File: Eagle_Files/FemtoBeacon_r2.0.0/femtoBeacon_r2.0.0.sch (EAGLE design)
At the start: 60 parts

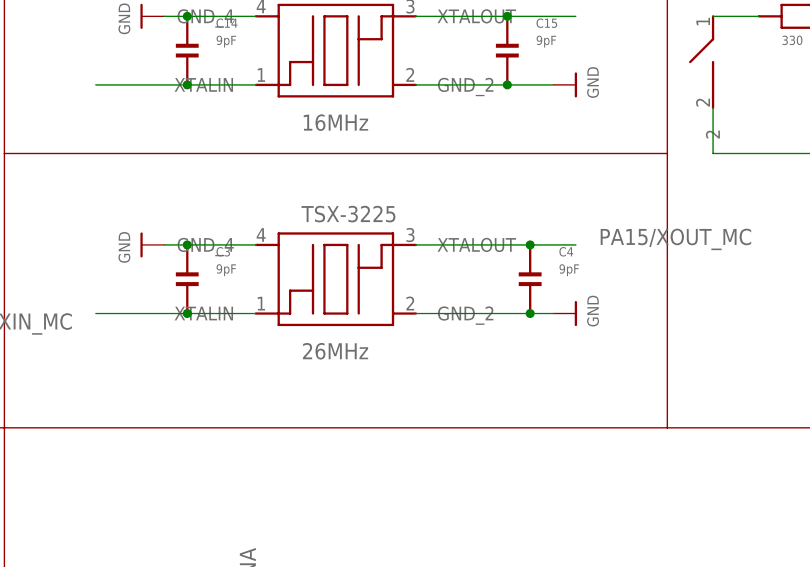
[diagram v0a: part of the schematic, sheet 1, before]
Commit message: Committing current work on FemtoBeacon (zigbee/mesh) r2.0.1, and USB dongle
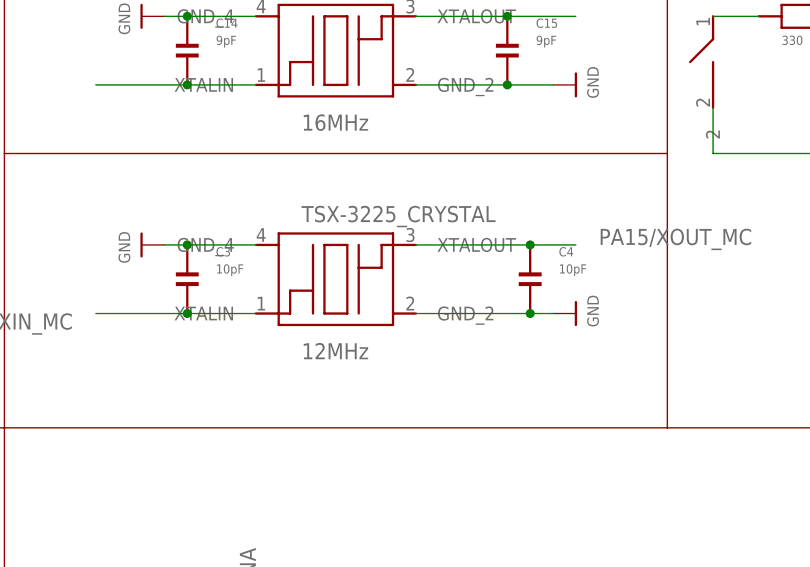
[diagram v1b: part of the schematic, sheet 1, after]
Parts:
- C3, C4: value 9pF -> 10pF
- TSX-3225_CRYSTAL: value 26MHz -> 12MHz
- renumbered TSX-3225 to TSX-3225_CRYSTAL, U$8 to USB
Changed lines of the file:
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@@
 <?xml version="1.0" encoding="utf-8"?>
 <!DOCTYPE eagle SYSTEM "eagle.dtd">
-<eagle version="6.5.0">
+<eagle version="7.5.0">
 <drawing>
 <settings>
@@
 </part>
 <part name="U$87" library="microbuilder" deviceset="3.3V" device=""/>
-<part name="TSX-3225" library="crystals" deviceset="TSX-3225" device="" value="26MHz"/>
+<part name="TSX-3225_CRYSTAL" library="crystals" deviceset="TSX-3225" device="" value="12MHz"/>
 <part name="U$20" library="microbuilder" deviceset="GND" device=""/>
 <part name="U$21" library="microbuilder" deviceset="GND" device=""/>
-<part name="C3" library="parts_0201" deviceset="CAPACITOR_0201" device="" value="9pF">
-<attribute name="DIGIKEY_PART" value="490-3194-1-ND"/>
-</part>
-<part name="C4" library="parts_0201" deviceset="CAPACITOR_0201" device="" value="9pF">
+<part name="C3" library="parts_0201" deviceset="CAPACITOR_0201" device="" value="10pF">
+<attribute name="DIGIKEY_PART" value="490-3194-1-ND"/>
+</part>
+<part name="C4" library="parts_0201" deviceset="CAPACITOR_0201" device="" value="10pF">
 <attribute name="DIGIKEY_PART" value="490-3194-1-ND"/>
 </part>
@@
 <part name="U$94" library="microbuilder" deviceset="GND" device=""/>
 <part name="U$89" library="microbuilder" deviceset="3.3V" device=""/>
-<part name="U$8" library="femtoduino" deviceset="USB_MICROB" device=""/>
+<part name="USB" library="femtoduino" deviceset="USB_MICROB" device=""/>
 <part name="FB1" library="microbuilder" deviceset="FERRITE" device="_0603MP"/>
 <part name="U$11" library="microbuilder" deviceset="VIN" device=""/>
@@
 </instance>
 <instance part="U$87" gate="G$1" x="205.74" y="71.12"/>
-<instance part="TSX-3225" gate="G$1" x="167.64" y="124.46"/>
+<instance part="TSX-3225_CRYSTAL" gate="G$1" x="167.64" y="124.46"/>
 <instance part="U$20" gate="G$1" x="195.58" y="121.92" rot="R90"/>
 <instance part="U$21" gate="G$1" x="147.32" y="129.54" rot="R270"/>
@@
 <instance part="U$52" gate="G$1" x="195.58" y="147.32" rot="R90"/>
 <instance part="U$51" gate="G$1" x="63.5" y="73.66"/>
-<instance part="U$8" gate="G$1" x="15.24" y="20.32"/>
+<instance part="USB" gate="G$1" x="15.24" y="20.32"/>
 <instance part="FB1" gate="G$1" x="27.94" y="15.24"/>
 <instance part="U$11" gate="G$1" x="22.86" y="25.4" rot="R270"/>
@@
 </segment>
 <segment>
-<pinref part="TSX-3225" gate="G$1" pin="XTALIN"/>
+<pinref part="TSX-3225_CRYSTAL" gate="G$1" pin="XTALIN"/>
 <wire x1="160.02" y1="121.92" x2="152.4" y2="121.92" width="0.1524" layer="91"/>
 <label x="139.7" y="121.92" size="1.778" layer="95" rot="R180"/>
@@
 </segment>
 <segment>
-<pinref part="TSX-3225" gate="G$1" pin="XTALOUT"/>
+<pinref part="TSX-3225_CRYSTAL" gate="G$1" pin="XTALOUT"/>
 <wire x1="177.8" y1="129.54" x2="190.5" y2="129.54" width="0.1524" layer="91"/>
 <label x="198.12" y="129.54" size="1.778" layer="95"/>
@@
 </segment>
 <segment>
-<pinref part="U$8" gate="G$1" pin="D-"/>
+<pinref part="USB" gate="G$1" pin="D-"/>
 <wire x1="15.24" y1="22.86" x2="27.94" y2="22.86" width="0.1524" layer="91"/>
 <label x="30.48" y="22.86" size="1.778" layer="95"/>
@@
 </segment>
 <segment>
-<pinref part="U$8" gate="G$1" pin="D+"/>
+<pinref part="USB" gate="G$1" pin="D+"/>
 <wire x1="15.24" y1="20.32" x2="27.94" y2="20.32" width="0.1524" layer="91"/>
 <label x="30.48" y="20.32" size="1.778" layer="95"/>
@@
 </segment>
 <segment>
-<pinref part="TSX-3225" gate="G$1" pin="GND_2"/>
+<pinref part="TSX-3225_CRYSTAL" gate="G$1" pin="GND_2"/>
 <wire x1="177.8" y1="121.92" x2="190.5" y2="121.92" width="0.1524" layer="91"/>
 <pinref part="U$20" gate="G$1" pin="GND"/>
@@
 </segment>
 <segment>
-<pinref part="TSX-3225" gate="G$1" pin="GND_4"/>
+<pinref part="TSX-3225_CRYSTAL" gate="G$1" pin="GND_4"/>
 <wire x1="160.02" y1="129.54" x2="152.4" y2="129.54" width="0.1524" layer="91"/>
 <pinref part="U$21" gate="G$1" pin="GND"/>
@@
 </segment>
 <segment>
-<pinref part="U$8" gate="G$1" pin="V"/>
+<pinref part="USB" gate="G$1" pin="V"/>
 <wire x1="15.24" y1="25.4" x2="20.32" y2="25.4" width="0.1524" layer="91"/>
 <pinref part="U$11" gate="G$1" pin="VIN"/>
@@
 <net name="N$5" class="0">
 <segment>
-<pinref part="U$8" gate="G$1" pin="GND@2"/>
+<pinref part="USB" gate="G$1" pin="GND@2"/>
 <junction x="2.54" y="7.62"/>
-<pinref part="U$8" gate="G$1" pin="GND@3"/>
+<pinref part="USB" gate="G$1" pin="GND@3"/>
 <junction x="5.08" y="7.62"/>
 <wire x1="2.54" y1="7.62" x2="5.08" y2="7.62" width="0.1524" layer="91"/>
-<pinref part="U$8" gate="G$1" pin="GND@4"/>
+<pinref part="USB" gate="G$1" pin="GND@4"/>
 <junction x="7.62" y="7.62"/>
 <wire x1="5.08" y1="7.62" x2="7.62" y2="7.62" width="0.1524" layer="91"/>
-<pinref part="U$8" gate="G$1" pin="GND@5"/>
+<pinref part="USB" gate="G$1" pin="GND@5"/>
 <junction x="10.16" y="7.62"/>
 <wire x1="7.62" y1="7.62" x2="10.16" y2="7.62" width="0.1524" layer="91"/>
-<pinref part="U$8" gate="G$1" pin="GND@6"/>
+<pinref part="USB" gate="G$1" pin="GND@6"/>
 <junction x="12.7" y="7.62"/>
 <wire x1="10.16" y1="7.62" x2="12.7" y2="7.62" width="0.1524" layer="91"/>
-<pinref part="U$8" gate="G$1" pin="GND@7"/>
+<pinref part="USB" gate="G$1" pin="GND@7"/>
 <junction x="15.24" y="7.62"/>
 <wire x1="12.7" y1="7.62" x2="15.24" y2="7.62" width="0.1524" layer="91"/>
@@
 <wire x1="20.32" y1="15.24" x2="25.4" y2="15.24" width="0.1524" layer="91"/>
 <junction x="20.32" y="15.24"/>
-<pinref part="U$8" gate="G$1" pin="GND@1"/>
+<pinref part="USB" gate="G$1" pin="GND@1"/>
 <wire x1="15.24" y1="15.24" x2="20.32" y2="15.24" width="0.1524" layer="91"/>
 <pinref part="FB1" gate="G$1" pin="P$1"/>
